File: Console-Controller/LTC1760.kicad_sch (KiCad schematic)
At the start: 71 parts, among them J5 Battery, J6 Battery, Q6 Si7141DP, Q7 Si7141DP, U12 FDS6990, U13 LTC1760, U14 FDS4935BZ, U15 FDS4935BZ, U16 FDS4935BZ, U17 FDS6990, U7 FDS6990

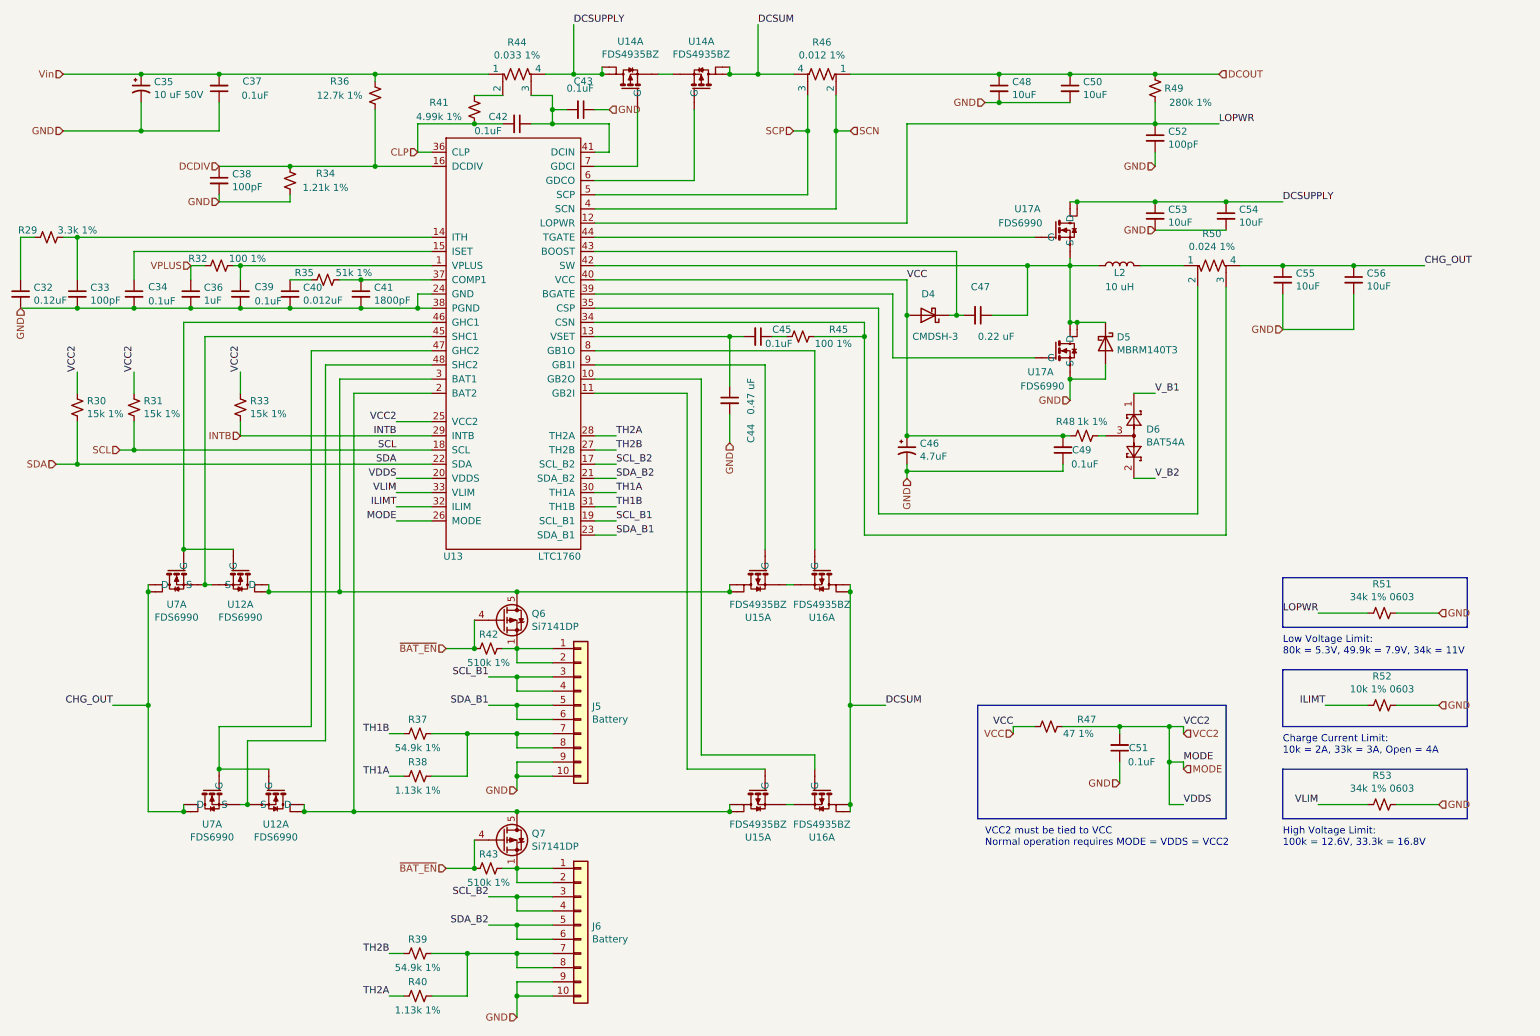
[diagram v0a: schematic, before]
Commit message: fixed bug in LTC1760 full-discharge rechrage mode, missing V_Batt
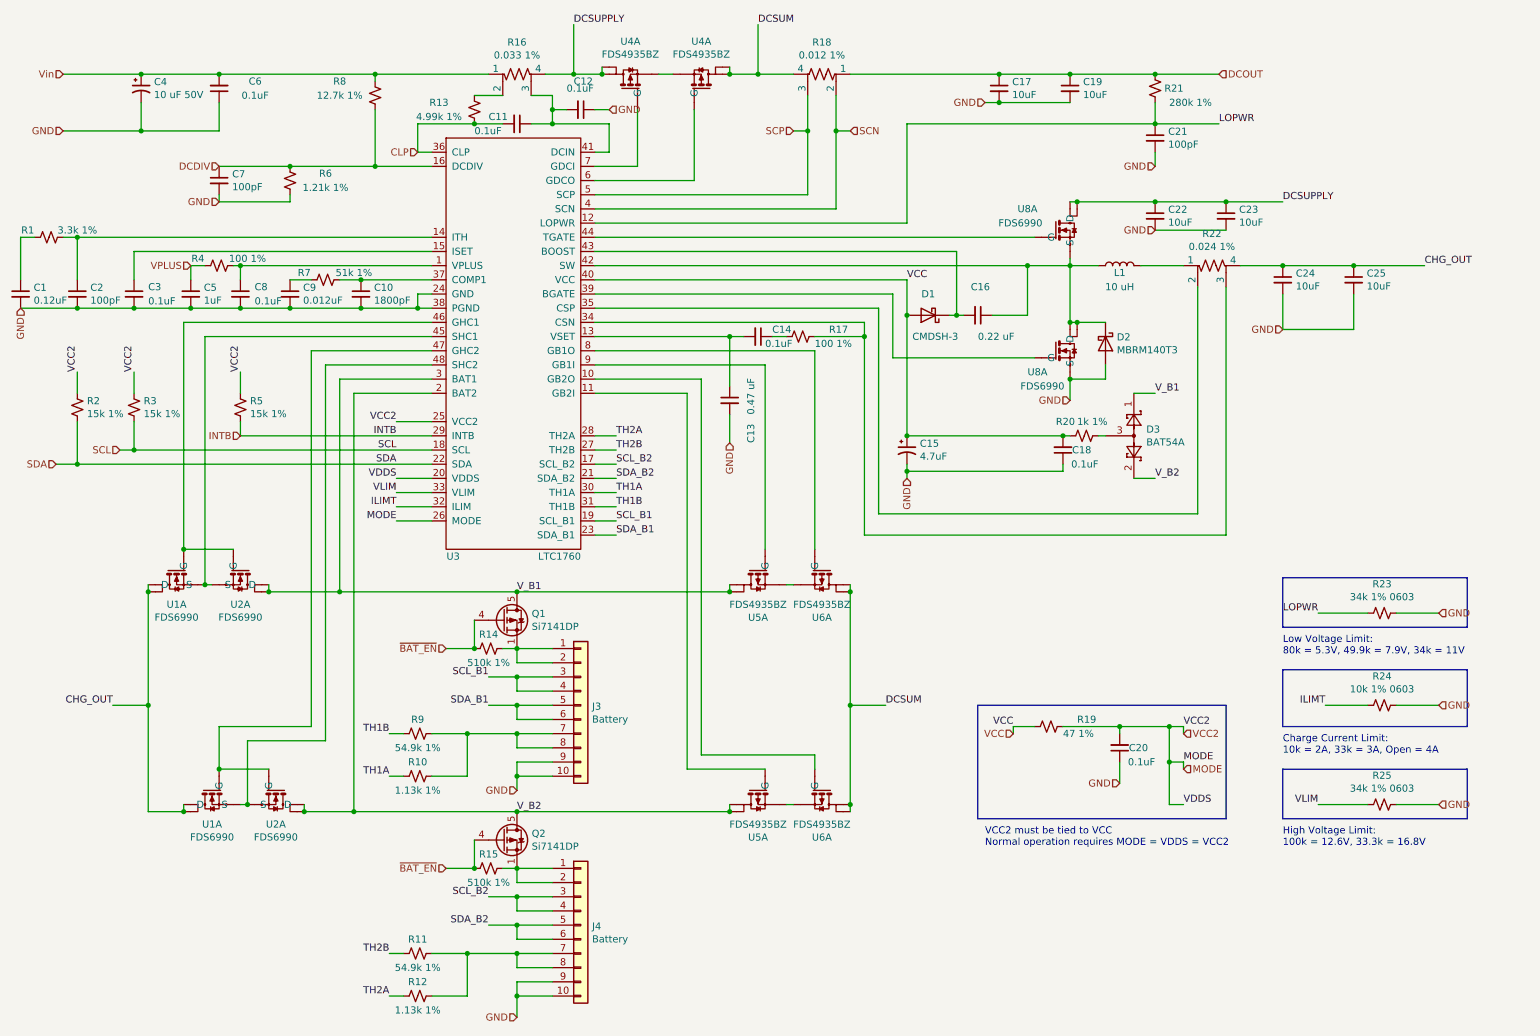
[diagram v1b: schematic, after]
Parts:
- renumbered C32 to C1, C41 to C10, C42 to C11, C43 to C12, C44 to C13, C45 to C14, C46 to C15, C47 to C16, C48 to C17, C49 to C18, C50 to C19, C33 to C2, C51 to C20, C52 to C21, C53 to C22, C54 to C23, C55 to C24, C56 to C25, C34 to C3, C35 to C4, C36 to C5, C37 to C6, C38 to C7, C39 to C8, C40 to C9, D4 to D1, D5 to D2, D6 to D3, J5 to J3, J6 to J4, L2 to L1, Q6 to Q1, Q7 to Q2, R29 to R1, R38 to R10, R39 to R11, R40 to R12, R41 to R13, R42 to R14, R43 to R15, R44 to R16, R45 to R17, R46 to R18, R47 to R19, R30 to R2, R48 to R20, R49 to R21, R50 to R22, R51 to R23, R52 to R24, R53 to R25, R31 to R3, R32 to R4, R33 to R5, R34 to R6, R35 to R7, R36 to R8, R37 to R9, U7 to U1, U12 to U2, U13 to U3, U14 to U4, U15 to U5, U16 to U6, U17 to U8
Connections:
- net V_B1: now also Q1.5 (D), U2.7 (D), U2.8 (D), U3.3 (BAT1), U5.7 (D), U5.8 (D)
- net V_B2: now also Q2.5 (D), U2.7 (D), U2.8 (D), U3.2 (BAT2), U5.7 (D), U5.8 (D)

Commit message: latest WIP, LTC1760 module ready for layout, strone-controller ready for layout but needs mech board drawings
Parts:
- renumbered C8 to C?, C2 to C?, C9 to C?, C10 to C?, C5 to C?, C1 to C?, C3 to C?, C11 to C?, C7 to C?, C12 to C?, C6 to C?, C17 to C?, C19 to C?, C22 to C?, C23 to C?, C24 to C?, C25 to C?, C16 to C?, C15 to C?, C13 to C?, C14 to C?, C18 to C?, C20 to C?, C21 to C?, C4 to C?, D3 to D?, D1 to D?, D2 to D?, J3 to J?, J4 to J?, L1 to L?, Q2 to Q?, Q1 to Q?, R9 to R?, R10 to R?, R11 to R?, R12 to R?, R5 to R?, R2 to R?, R3 to R?, R15 to R?, R14 to R?, R7 to R?, R1 to R?, R4 to R?, R8 to R?, R6 to R?, R13 to R?, R16 to R?, R22 to R?, R18 to R?, R24 to R?, R17 to R?, R20 to R?, R23 to R?, R25 to R?, R19 to R?, R21 to R?, U3 to U?, U4 to U?, U6 to U?, U8 to U?, U1 to U?, U2 to U?, U5 to U?
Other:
- company: Guatek -> (none)
- title: WW-Battery-Pack PCBs -> Console-Controller
